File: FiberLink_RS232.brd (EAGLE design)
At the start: 160 x 100 mm, 62 parts, among them IC1 MAX412CPAMSOP, IC2 MAX3232CSE, IC3 74LVC1G08DBV, IC4 FT232BL, K1 629105136821, Q1 XTAL_3225_SMD, U1 SN65HVD3088EDMSOP

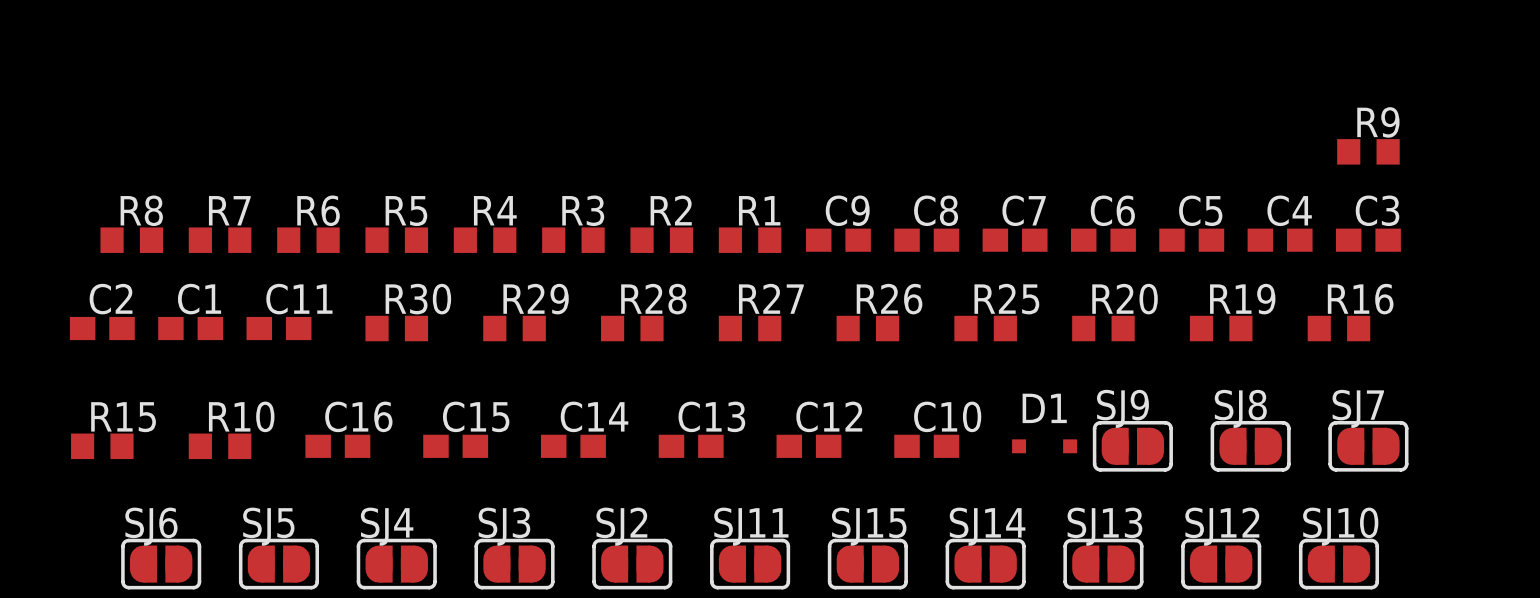
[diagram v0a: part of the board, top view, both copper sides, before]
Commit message: changed passive packages
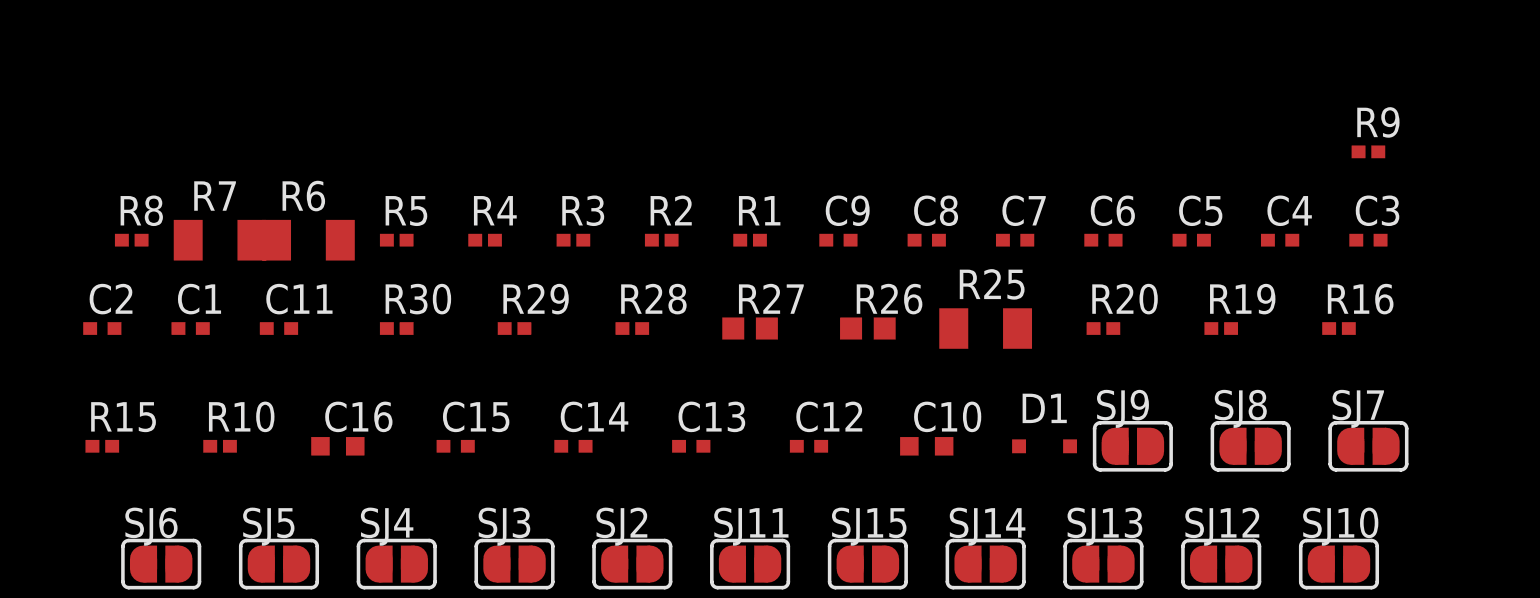
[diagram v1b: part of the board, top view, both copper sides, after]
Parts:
- C1, C11, C12, C13, C14, C15, C2, C3, C4, C5, C6, C7, C8, C9: device rcl:C0603 -> rcl:C0402
- R1, R10, R15, R16, R19, R2, R20, R28, R29, R3, R30, R4, R5, R8, R9: device rcl:R0603 -> rcl:R0402_VISHAY
- R25, R6, R7: device rcl:R0603 -> rcl:R1206

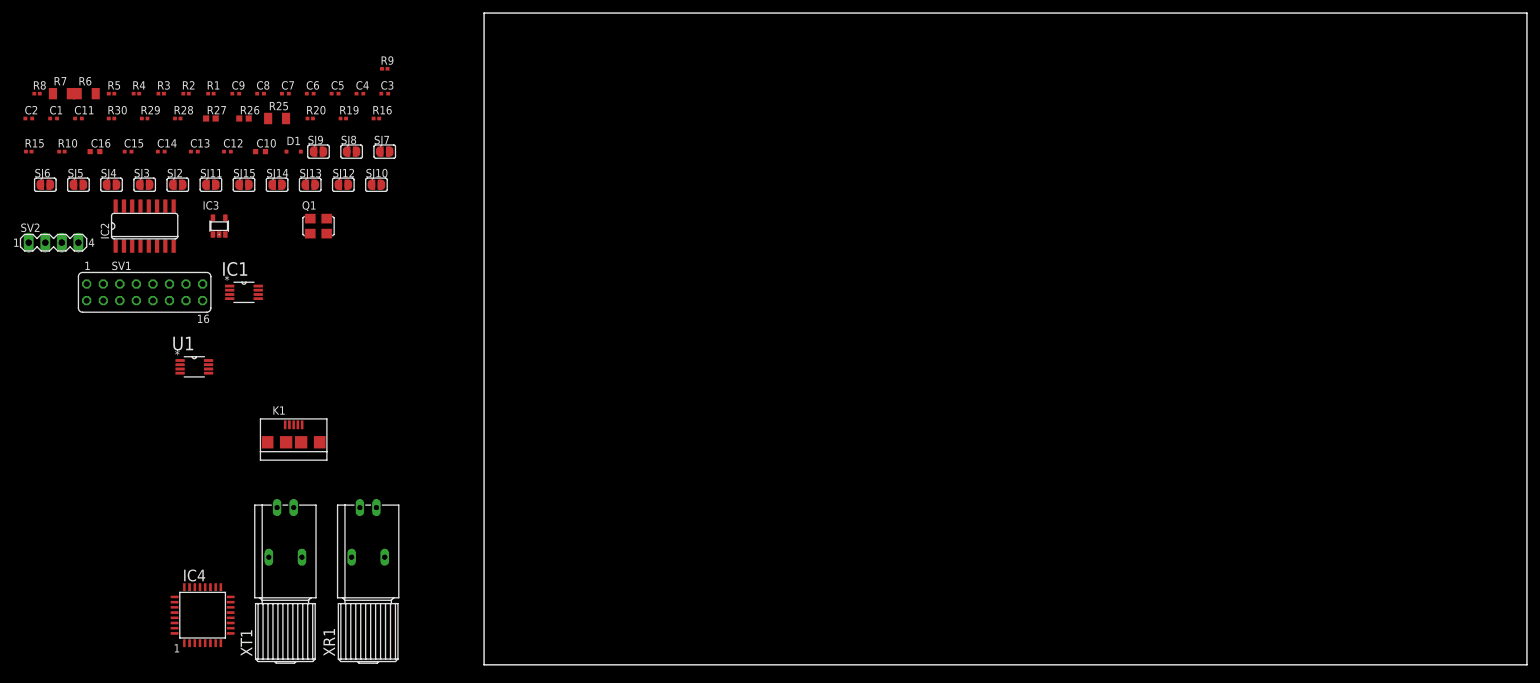
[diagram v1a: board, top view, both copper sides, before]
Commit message: first completely routed
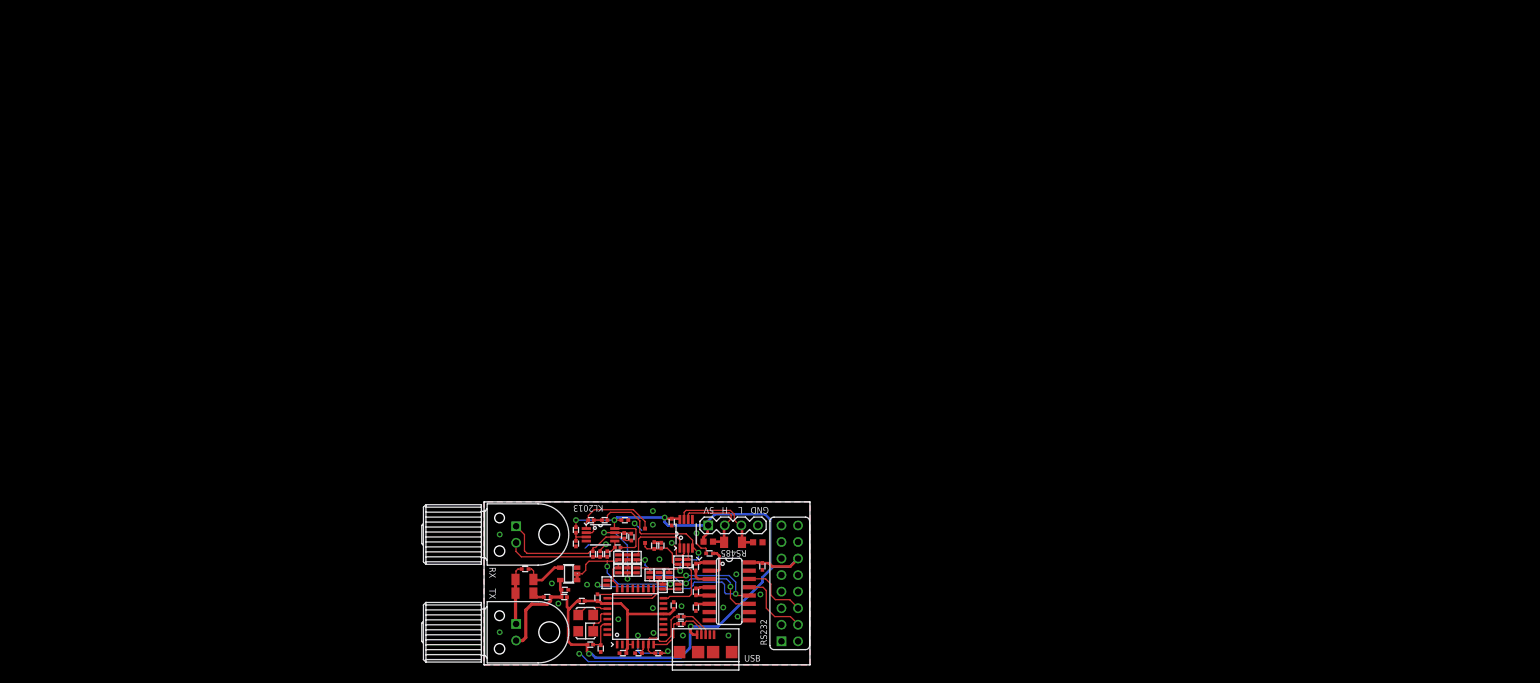
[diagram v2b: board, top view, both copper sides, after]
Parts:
- removed IC1: MAX412CPAMSOP, OMAT_IC:SOP65P490X110-8N
- removed IC2: MAX3232CSE, maxim:SO16
- removed IC3: 74LVC1G08DBV, 74xx-little-us:SOT23-5
- removed IC4: FT232BL, ftdichip-3:LQFP32
- removed K1: 629105136821, OMAT_IC:629105136821
- removed Q1: XTAL_3225_SMD, OMAT_IC:X_3225
- removed R20: (no value), rcl:R0402_VISHAY
- removed SV1: (no value), con-lsta:FE08-2
- removed SV2: (no value), con-lstb:MA04-1
- removed U1: SN65HVD3088EDMSOP, OMAT_IC:SOP65P490X110-8N
- removed XR1: SFH250V, OMAT_IC:SFH-V
- removed XT1: SFH450V, OMAT_IC:SFH-V
- added C17: (no value), rcl:C0402
- added D2: MAX3232CSE, maxim:SO16
- added D3: 74LVC1G08DBV, 74xx-little-us:SOT23-5
- added D4: FT232BL, ftdichip-3:LQFP32
- added G1: XTAL_3225_SMD, OMAT_IC:X_3225
- added H1: IFE91A, OMAT_IC:IFO-IFX
- added L1, L2: (no value), rcl:R0402_VISHAY
- added N1: MAX412CPAMSOP, OMAT_IC:SOP65P490X110-8N
- added V1: IFD91, OMAT_IC:IFO-IFX
- added V2: (no value), diode:SOD323-R
- added X1: 629105136821, OMAT_IC:629105136821
- added X2: (no value), OMAT_IC:FE08-2
- added X3: (no value), OMAT_IC:MA04-1
- C10, C16: device rcl:C0603 -> rcl:C0402
- D1: value (none) -> SN65HVD3088EDMSOP; device diode:SOD323-R -> OMAT_IC:SOP65P490X110-8N
- SJ10, SJ11, SJ12, SJ13, SJ14, SJ15, SJ2, SJ3, SJ4, SJ5, SJ6, SJ7, SJ8, SJ9: device OMAT_IC:SJ -> OMAT_IC:SJ-SMALL
- moved R15 123.5 mm to (30.2, 6.30), turned to 180 degrees
- moved C11 118.8 mm to (23.7, 1.80), turned to 180 degrees
- moved SJ6 115.0 mm to (29.8, 12.0), turned to 90 degrees
- moved R10 110.9 mm to (16.3, 3.10)
- moved C2 110.3 mm to (21.6, 22.2), turned to 180 degrees
- moved C1 109.5 mm to (22.6, 19.6), turned to 90 degrees
- moved SJ5 108.8 mm to (27.4, 12.0), turned to 270 degrees
- moved R8 107.3 mm to (16.4, 22.2)
- moved R30 106.8 mm to (27.2, 18.3), turned to 90 degrees
- moved C14 105.0 mm to (29.1, 9.10), turned to 90 degrees
- moved C16 104.9 mm to (26.1, 18.3), turned to 270 degrees
- moved R5 103.8 mm to (18.9, 17.0), turned to 90 degrees
- moved SJ4 103.1 mm to (26.8, 13.8), turned to 90 degrees
- moved C7 103.0 mm to (42.7, 15.1), turned to 270 degrees
- moved R7 102.9 mm to (6.20, 13.1), turned to 180 degrees
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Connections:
- removed net N$18: C10.1, IC4.30, R10.2
- removed net N$20: IC3.1, IC3.2, SJ4.1, SJ5.1, SJ8.1
- removed net N$22: C12.1, C13.1, C14.1, IC4.13, IC4.26, IC4.3, IC4.4, R20.2
- removed net N$25: IC4.24, SJ10.1, SJ3.2, SJ7.1
- removed net N$26: IC2.11, SJ13.1, SJ2.2, SJ6.2
- removed net N$27: IC2.12, SJ12.1, SJ4.2, SJ7.2
- removed net N$28: IC4.25, SJ11.1, SJ5.2, SJ6.1
- removed net N$30: C11.1, IC4.6
- removed net N$31: C16.2, D1.C, R30.1, SJ14.1
- removed net N$34: IC4.27, Q1.3
- removed net N$35: SJ10.2, SJ13.2, SJ8.2, U1.1
- removed net N$37: SJ14.2, SJ15.2, U1.3
- removed net N$38: R25.2, R26.1, SV2.3, U1.7
- removed net N$39: R25.1, R27.2, SV2.2, U1.6
- removed net N$4: C1.2, IC1.7, R4.1, SJ2.1, SJ3.1, SJ9.1
- removed net N$40: IC4.16, SJ15.1
- removed net N$41: R29.2, SJ11.2, SJ12.2, SJ9.2, U1.4
- new net 485_HIGH: D1.6, R25.1, R27.2, X3.2
- new net 485_LOW: D1.7, R25.2, R26.1, X3.3
- new net AVCC: C10.1, D4.30, R10.2
- new net CARRIER_SENSE: C16.2, R30.1, SJ14.1, V2.C
- new net G1: D4.27, G1.3
- new net RXD_232: D2.12, SJ12.1, SJ4.2, SJ7.2
- new net RXD_485: D1.1, SJ10.2, SJ13.2, SJ8.2
- new net RXD_FIBER: C1.2, N1.7, R4.1, SJ2.1, SJ3.1, SJ9.1
- new net RXD_USB: D4.24, SJ10.1, SJ3.2, SJ7.1
- new net TXD_232: D2.11, SJ13.1, SJ2.2, SJ6.2
- new net TXD_485: D1.4, R29.2, SJ11.2, SJ12.2, SJ9.2
- new net TXD_FIBER: D3.1, D3.2, SJ4.1, SJ5.1, SJ8.1
- new net TXD_USB: D4.25, SJ11.1, SJ5.2, SJ6.1
- new net TXEN_485: D1.3, SJ14.2, SJ15.2
- new net TXEN_USB: D4.16, SJ15.1
- new net TX_VCC: C17.1, C8.1, D3.5, H1.2, L2.1
- new net USB3V3: C11.1, D4.6
- new net USBVCC: C12.1, C13.1, C14.1, D4.13, D4.26, D4.3, D4.4, L1.2
- net +5V: now also D1.8, D2.16, L1.1, L2.2, N1.8, X1.1, X2.12, X3.1; no longer C8.1, IC1.8, IC2.16, IC3.5, K1.1, R20.1, SV1.12, SV2.1, U1.8, XT1.A
- net GND: now also C17.2, D1.2, D1.5, D2.15, D3.3, D4.14, D4.17, D4.29, D4.31, D4.9, N1.4, X1.5, X1.Z1, X1.Z2, X1.Z3, X1.Z4, X2.14, X2.16, X2.2, X3.4; no longer IC1.4, IC2.15, IC3.3, IC4.14, IC4.17, IC4.29, IC4.31, IC4.9, K1.5, K1.Z1, K1.Z2, K1.Z3, K1.Z4, SV1.14, SV1.16, SV1.2, SV2.4, U1.2, U1.5
- net N$1: now also N1.6, V1.1; no longer IC1.6, XR1.K
- net N$10: now also D2.6; no longer IC2.6
- net N$11: now also D2.2; no longer IC2.2
- net N$12: now also D2.14, X2.6; no longer IC2.14, SV1.6
- net N$13: now also D2.13, X2.4; no longer IC2.13, SV1.4
- net N$15: now also H1.1; no longer XT1.K
- net N$16: now also N1.3; no longer IC1.3
- net N$17: now also D3.4; no longer IC3.4
- net N$19: now also X1.2; no longer K1.2
- net N$2: now also N1.1, V2.A; no longer D1.A, IC1.1
- net N$21: now also D4.8; no longer IC4.8
- net N$23: now also D4.7; no longer IC4.7
- net N$24: now also X1.3; no longer K1.3
- net N$29: now also D4.5; no longer IC4.5
- net N$3: now also V1.2; no longer XR1.A
- net N$32: now also N1.2; no longer IC1.2
- net N$33: now also D4.28, G1.1; no longer IC4.28, Q1.1
- net N$5: now also N1.5; no longer IC1.5
- net N$6: now also D2.5; no longer IC2.5
- net N$7: now also D2.4; no longer IC2.4
- net N$8: now also D2.3; no longer IC2.3
- net N$9: now also D2.1; no longer IC2.1
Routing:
- net +5V: track 0.00 -> 121.9 mm, vias 0 -> 5
- net GND: track 0.00 -> 44.2 mm, vias 0 -> 23
- net RXD_232: track 0.00 -> 41.9 mm, vias 0 -> 3
- net TXD_485: track 0.00 -> 32.4 mm, vias 0 -> 2
- net TXD_232: track 0.00 -> 26.3 mm, vias 0 -> 3
- net TXD_FIBER: track 0.00 -> 23.5 mm, vias 0 -> 2
- net N$1: track 0.00 -> 22.4 mm
- net USBVCC: track 0.00 -> 22.3 mm
- net RXD_FIBER: track 0.00 -> 17.5 mm, vias 0 -> 2
- net N$3: track 0.00 -> 16.8 mm
- net 485_LOW: track 0.00 -> 15.8 mm
- net TX_VCC: track 0.00 -> 15.3 mm
- net TXD_USB: track 0.00 -> 14.7 mm
- net 485_HIGH: track 0.00 -> 14.0 mm
- net RXD_485: track 0.00 -> 13.2 mm
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- added copper zone on layer 1, net GND
- added copper zone on layer 16, net GND
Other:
- board size 160 x 100 mm -> 50 x 25 mm
- board text added: "(C) KL 2013"
- board text added: "5V"
- board text added: "FIBER"
- board text added: "FIBERLINK"
- board text added: "GND"
- board text added: "H"
- board text added: "KL2013"
- board text added: "L"
- board text added: "RS232"
- board text added: "RS485"
- board text added: "RX"
- board text added: "TX"
- board text added: "USB"
- board text added: "USB RS232 RS485 FIBER"

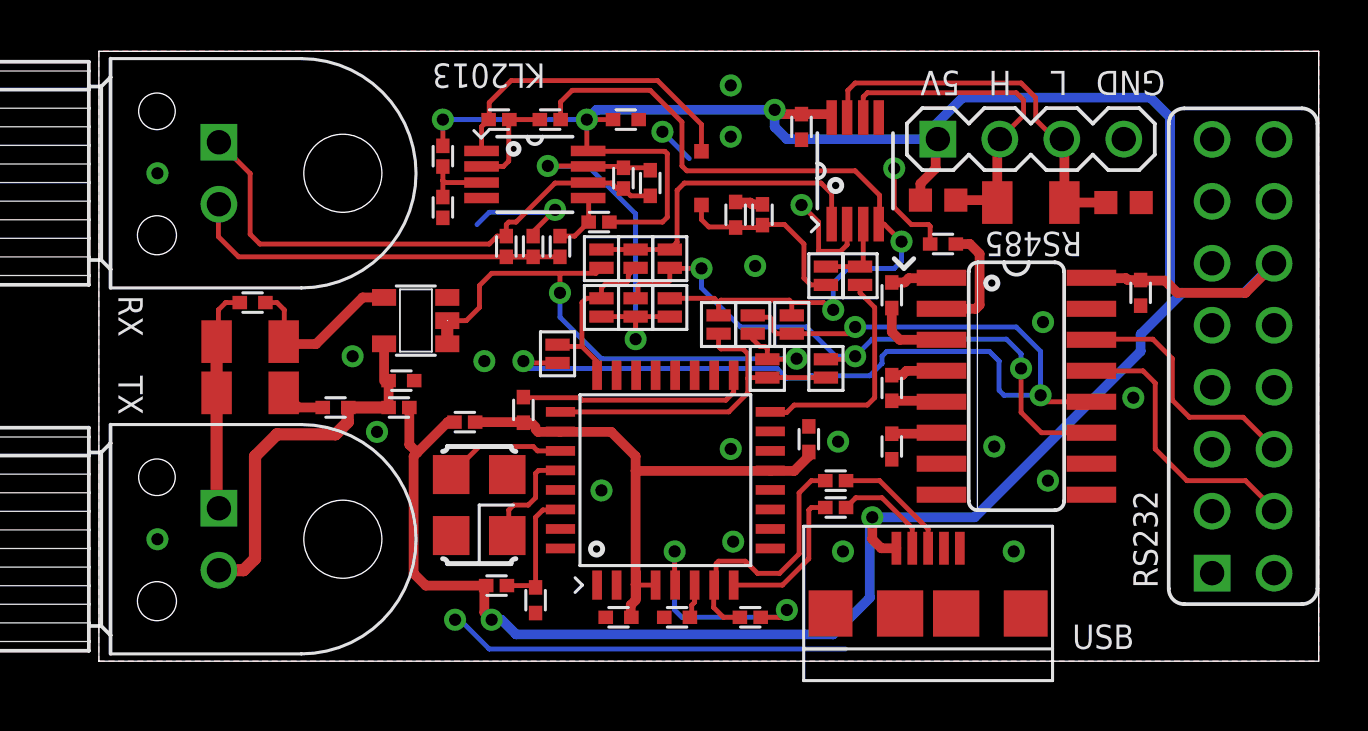
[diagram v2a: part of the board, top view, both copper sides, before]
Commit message: Added some leds
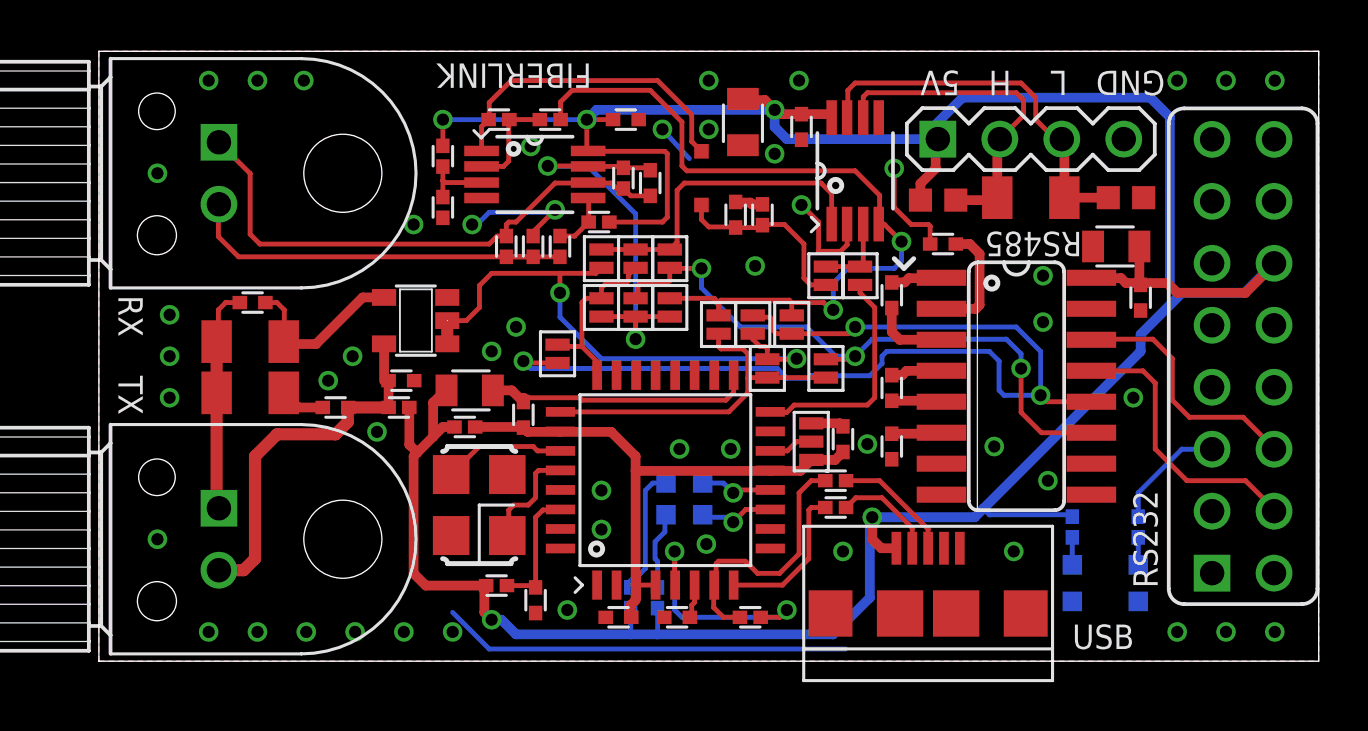
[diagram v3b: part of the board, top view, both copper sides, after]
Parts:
- added C18, C19, C20: (no value), rcl:C0805
- added H2, H3, H4, H5: (no value), OMAT_IC:CHIP-LED0603
- added R11, R12, R13, R14: (no value), rcl:R0402_VISHAY
- added SJ17: SJ-TRI, OMAT_IC:SJ-SMALL-TRI
- moved C14 1.40 mm to (30.5, 9.10)
- moved R26 0.22 mm to (42.1, 19.0)
- moved C12 0.20 mm to (17.4, 10.1)
- moved L1 0.20 mm to (15.0, 9.60)
- moved C7 0.20 mm to (42.7, 14.9)
- moved R25 0.20 mm to (38.2, 19.0)
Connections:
- new net FPGADONE: R14.1, X2.5
- new net N$14: D4.11, H4.C
- new net N$18: H3.A, R11.1
- new net N$20: H4.A, R12.1
- new net N$22: H2.A, R13.2
- new net N$25: H5.A, R14.2
- new net N$26: D4.14, SJ17.3
- new net N$4: D4.12, H3.C
- net +5V: now also C18.1, C19.1, C20.1, R11.2, R12.2, R13.1
- net GND: now also C18.2, C19.2, C20.2, H2.C, H5.C, SJ17.2; no longer D4.14
- net USBVCC: now also SJ17.1
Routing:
- net +5V: track 121.9 -> 133.1 mm
- net N$18: track 0.00 -> 5.26 mm
- net FPGADONE: track 0.00 -> 4.75 mm
- net N$20: track 0.00 -> 3.20 mm
- net N$14: track 0.00 -> 3.11 mm, vias 0 -> 1
- net N$4: track 0.00 -> 3.06 mm, vias 0 -> 1
- net GND: track 44.2 -> 47.1 mm, vias 23 -> 51
- net N$26: track 0.00 -> 1.84 mm
- net USBVCC: track 22.3 -> 23.5 mm
- net N$25: track 0.00 -> 1.12 mm
- net N$22: track 0.00 -> 1.12 mm
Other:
- board text added: "FPGADONE"
- board text added: "POWER"
- board text removed: "KL2013"
